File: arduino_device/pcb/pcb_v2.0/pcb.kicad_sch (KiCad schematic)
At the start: 3 parts, among them SW1 SW_Push

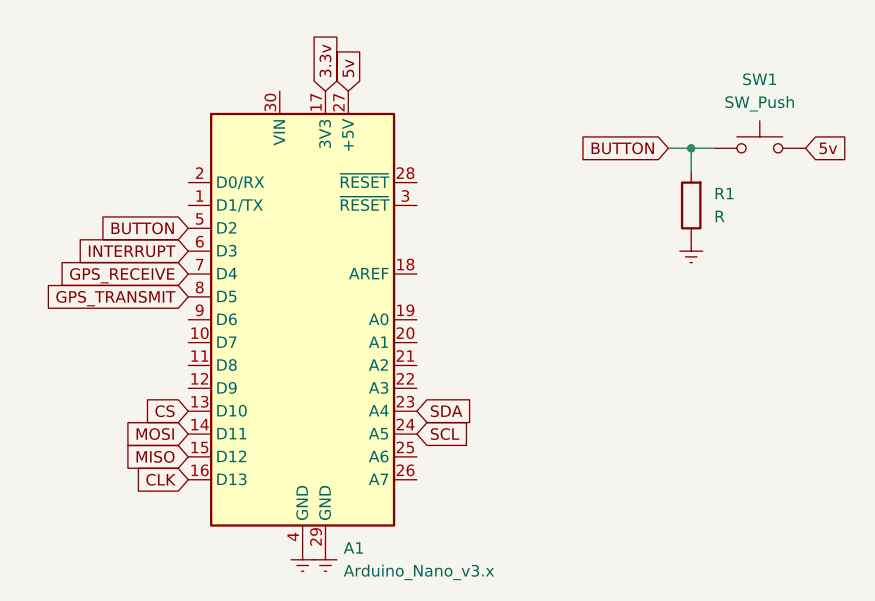
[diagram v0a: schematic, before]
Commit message: Arduino device -Test programs (Button, RTC, IMU, GPS) -Update PCB
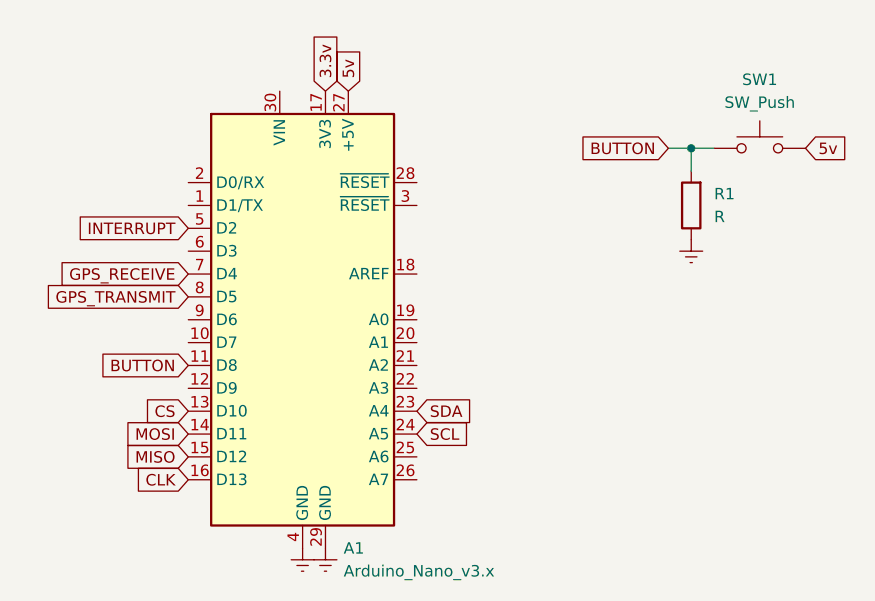
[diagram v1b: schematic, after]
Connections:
- net BUTTON: now also A1.11 (D8); no longer A1.5 (D2)
- net INTERRUPT: now also A1.5 (D2); no longer A1.6 (D3)
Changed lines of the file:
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@@
+    )
+  )
+  (global_label "INTERRUPT" (shape input) (at 119.38 81.28 180) (fields_autoplaced)
+    (effects (font (size 1.27 1.27)) (justify right))
+    (property "Intersheet References" "${INTERSHEET_REFS}" (id 0) (at 106.8069 81.2006 0)
+      (effects (font (size 1.27 1.27)) (justify right) hide)
     )
   )
@@
     )
   )
+  (global_label "BUTTON" (shape input) (at 119.38 96.52 180) (fields_autoplaced)
+    (effects (font (size 1.27 1.27)) (justify right))
+    (property "Intersheet References" "${INTERSHEET_REFS}" (id 0) (at 109.7702 96.4406 0)
+      (effects (font (size 1.27 1.27)) (justify right) hide)
+    )
+  )
   (global_label "SCL" (shape input) (at 144.78 104.14 0) (fields_autoplaced)
     (effects (font (size 1.27 1.27)) (justify left))
@@
       (effects (font (size 1.27 1.27)) (justify right) hide)
     )
-  )
-  (global_label "INTERRUPT" (shape input) (at 119.38 83.82 180) (fields_autoplaced)
-    (effects (font (size 1.27 1.27)) (justify right))
-    (property "Intersheet References" "${INTERSHEET_REFS}" (id 0) (at 106.8069 83.7406 0)
-      (effects (font (size 1.27 1.27)) (justify right) hide)
-    )
-  )
-  (global_label "BUTTON" (shape input) (at 119.38 81.28 180) (fields_autoplaced)
-    (effects (font (size 1.27 1.27)) (justify right))
-    (property "Intersheet References" "${INTERSHEET_REFS}" (id 0) (at 109.7702 81.2006 0)
-      (effects (font (size 1.27 1.27)) (justify right) hide)
-    )
